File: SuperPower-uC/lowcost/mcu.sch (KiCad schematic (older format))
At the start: 5 parts, among them J5 main pin header right, J6 main pin header left, U13 ESP32-WROOM32

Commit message: moved connector over to mcu sheet, made some vias smaller ...
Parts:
- removed J5: main pin header right, Connector_PinHeader_2.54mm:PinHeader_1x17_P2.54mm_Vertical, symbol Connector:Conn_01x17_Female
- removed J6: main pin header left, Connector_PinHeader_2.54mm:PinHeader_1x17_P2.54mm_Vertical, symbol Connector:Conn_01x17_Female
- added J5: main pin header fight, Connector_PinSocket_2.54mm:PinSocket_1x21_P2.54mm_Vertical, symbol Connector:Conn_01x21_Female
- added J6: main pin header left, Connector_PinSocket_2.54mm:PinSocket_1x21_P2.54mm_Vertical, symbol Connector:Conn_01x21_Female
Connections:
- net labels added: 3v3_EN, 5V_EN, CH_DIS, INT_IO, exp4, exp5, exp6, exp7
- wire segments 83 -> 91
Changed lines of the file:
@@
 IO23
 Wire Wire Line
-	9800 3250 9600 3250
-Wire Wire Line
-	9800 3350 9600 3350
-Wire Wire Line
-	9800 3450 9600 3450
-Wire Wire Line
-	9800 3550 9600 3550
-Wire Wire Line
-	9800 3650 9600 3650
-Wire Wire Line
-	9800 3750 9600 3750
-Wire Wire Line
-	9800 3950 9600 3950
-Wire Wire Line
-	9600 3850 9800 3850
-Wire Wire Line
-	9800 4050 9600 4050
-Wire Wire Line
-	9600 4150 9800 4150
-Wire Wire Line
-	9600 4250 9800 4250
-Text Label 9600 3250 0    50   ~ 0
+	9900 3550 9700 3550
+Wire Wire Line
+	9900 3650 9700 3650
+Wire Wire Line
+	9900 3750 9700 3750
+Wire Wire Line
+	9900 3850 9700 3850
+Wire Wire Line
+	9900 3950 9700 3950
+Wire Wire Line
+	9900 4050 9700 4050
+Wire Wire Line
+	9900 4250 9700 4250
+Wire Wire Line
+	9700 4150 9900 4150
+Wire Wire Line
+	9900 4350 9700 4350
+Wire Wire Line
+	9700 4450 9900 4450
+Wire Wire Line
+	9700 4550 9900 4550
+Text Label 9700 3550 0    50   ~ 0
 IO36
-Text Label 9600 3350 0    50   ~ 0
+Text Label 9700 3650 0    50   ~ 0
 IO39
-Text Label 9600 3450 0    50   ~ 0
+Text Label 9700 3750 0    50   ~ 0
 IO34
-Text Label 9600 3550 0    50   ~ 0
+Text Label 9700 3850 0    50   ~ 0
 IO35
-Text Label 9600 3650 0    50   ~ 0
+Text Label 9700 3950 0    50   ~ 0
 IO32
-Text Label 9600 3750 0    50   ~ 0
+Text Label 9700 4050 0    50   ~ 0
 IO33
-Text Label 9600 3850 0    50   ~ 0
+Text Label 9700 4150 0    50   ~ 0
 IO25
-Text Label 9600 3950 0    50   ~ 0
+Text Label 9700 4250 0    50   ~ 0
 IO26
-Text Label 9600 4050 0    50   ~ 0
+Text Label 9700 4350 0    50   ~ 0
 IO27
-Text Label 9600 4150 0    50   ~ 0
+Text Label 9700 4450 0    50   ~ 0
 IO14
-Text Label 9600 4250 0    50   ~ 0
+Text Label 9700 4550 0    50   ~ 0
 IO12
 Wire Wire Line
-	9800 4350 9600 4350
-Text Label 9600 4350 0    50   ~ 0
+	9900 4650 9700 4650
+Text Label 9700 4650 0    50   ~ 0
 IO13
 Wire Wire Line
-	9800 4450 9250 4450
+	9900 4750 9350 4750
 $Comp
 L power:GND #PWR0120
 U 1 1 5F8C9F4B
-P 9250 4450
-F 0 "#PWR0120" H 9250 4200 50  0001 C CNN
-F 1 "GND" H 9255 4277 50  0000 C CNN
-F 2 "" H 9250 4450 50  0001 C CNN
-F 3 "" H 9250 4450 50  0001 C CNN
-	1    9250 4450
-	1    0    0    -1
-$EndComp
-Wire Wire Line
-	9600 1250 9800 1250
-Wire Wire Line
-	9600 1350 9800 1350
-Wire Wire Line
-	9600 1450 9800 1450
-Wire Wire Line
-	9600 1550 9800 1550
-Wire Wire Line
-	9600 1650 9800 1650
-Wire Wire Line
-	9600 1750 9800 1750
-Wire Wire Line
-	9600 1850 9800 1850
-Wire Wire Line
-	9600 1950 9800 1950
-Wire Wire Line
-	9600 2050 9800 2050
-Wire Wire Line
-	9600 2150 9800 2150
-Wire Wire Line
-	9600 2250 9800 2250
-Wire Wire Line
-	9600 1150 9800 1150
-Text Label 9600 1150 0    50   ~ 0
+P 9350 4750
+F 0 "#PWR0120" H 9350 4500 50  0001 C CNN
+F 1 "GND" H 9355 4577 50  0000 C CNN
+F 2 "" H 9350 4750 50  0001 C CNN
+F 3 "" H 9350 4750 50  0001 C CNN
+	1    9350 4750
+	1    0    0    -1
+$EndComp
+Wire Wire Line
+	9700 1150 9900 1150
+Wire Wire Line
+	9700 1250 9900 1250
+Wire Wire Line
+	9700 1350 9900 1350
+Wire Wire Line
+	9700 1450 9900 1450
+Wire Wire Line
+	9700 1550 9900 1550
+Wire Wire Line
+	9700 1650 9900 1650
+Wire Wire Line
+	9700 1750 9900 1750
+Wire Wire Line
+	9700 1850 9900 1850
+Wire Wire Line
+	9700 1950 9900 1950
+Wire Wire Line
+	9700 2050 9900 2050
+Wire Wire Line
+	9700 2150 9900 2150
+Wire Wire Line
+	9700 1050 9900 1050
+Text Label 9700 1050 0    50   ~ 0
 IO0
-Text Label 9600 2250 0    50   ~ 0
+Text Label 9700 2150 0    50   ~ 0
 IO4
-Text Label 9600 2150 0    50   ~ 0
+Text Label 9700 2050 0    50   ~ 0
 IO16
-Text Label 9600 2050 0    50   ~ 0
+Text Label 9700 1950 0    50   ~ 0
 IO17
-Text Label 9600 1950 0    50   ~ 0
+Text Label 9700 1850 0    50   ~ 0
 IO5
-Text Label 9600 1850 0    50   ~ 0
+Text Label 9700 1750 0    50   ~ 0
 IO18
-Text Label 9600 1750 0    50   ~ 0
+Text Label 9700 1650 0    50   ~ 0
 IO19
-Text Label 9600 1650 0    50   ~ 0
+Text Label 9700 1550 0    50   ~ 0
 IO21
-Text Label 9600 1550 0    50   ~ 0
+Text Label 9700 1450 0    50   ~ 0
 RX
-Text Label 9600 1450 0    50   ~ 0
+Text Label 9700 1350 0    50   ~ 0
 TX
-Text Label 9600 1350 0    50   ~ 0
+Text Label 9700 1250 0    50   ~ 0
 IO22
-Text Label 9600 1250 0    50   ~ 0
+Text Label 9700 1150 0    50   ~ 0
 IO23
 Wire Wire Line
-	9800 2350 9600 2350
-Text Label 9600 2350 0    50   ~ 0
+	9900 2250 9700 2250
+Text Label 9700 2250 0    50   ~ 0
 IO2
 Text Label 1250 1150 0    50   ~ 0
@@
 	1150 1750 1250 1750
 Wire Wire Line
-	9800 2450 9600 2450
-Text Label 9600 2450 0    50   ~ 0
+	9900 2350 9700 2350
+Text Label 9700 2350 0    50   ~ 0
 IO15
 Text HLabel 1100 2200 0    50   Input ~ 0
@@
 	11000 700  9000 700
 Wire Notes Line
-	9000 700  9000 5000
-Wire Notes Line
-	9000 5000 11000 5000
-Wire Notes Line
-	11000 700  11000 5000
+	9000 5450 11000 5450
 Wire Notes Line
 	3400 2300 8000 2300
@@
 Text Notes 3500 2450 0    50   ~ 0
 MCU
-Text Label 9400 4650 0    50   ~ 0
+Text Label 9500 4950 0    50   ~ 0
 5V
 Wire Wire Line
-	9800 2650 9400 2650
-Text Label 9400 2650 0    50   ~ 0
+	9900 2550 9500 2550
+Text Label 9500 2550 0    50   ~ 0
 3v3_MCU
 Text Label 3950 3250 0    50   ~ 0
@@
 5V
 Wire Wire Line
-	9400 4650 9800 4650
+	9500 4950 9900 4950
 Wire Notes Line
 	600  650  1850 650
@@
 Text Notes 9100 850  0    50   ~ 0
 Main pin Headers\n
-Text Label 9600 3150 0    50   ~ 0
+Text Label 9700 3450 0    50   ~ 0
 RST
 Wire Wire Line
-	9600 3150 9800 3150
-Wire Wire Line
-	9800 2550 9250 2550
+	9700 3450 9900 3450
+Wire Wire Line
+	9900 2450 9350 2450
 $Comp
 L power:GND #PWR0119
 U 1 1 5F8D40E5
-P 9250 2550
-F 0 "#PWR0119" H 9250 2300 50  0001 C CNN
-F 1 "GND" H 9255 2377 50  0000 C CNN
-F 2 "" H 9250 2550 50  0001 C CNN
-F 3 "" H 9250 2550 50  0001 C CNN
-	1    9250 2550
-	1    0    0    -1
-$EndComp
-$Comp
-L Connector:Conn_01x17_Female J5
-U 1 1 5F904645
-P 10000 1950
-F 0 "J5" H 10028 1976 50  0000 L CNN
-F 1 "main pin header right" H 10028 1885 50  0000 L CNN
-F 2 "Connector_PinHeader_2.54mm:PinHeader_1x17_P2.54mm_Vertical" H 10000 1950 50  0001 C CNN
-F 3 "~" H 10000 1950 50  0001 C CNN
-	1    10000 1950
-	1    0    0    -1
-$EndComp
-$Comp
-L Connector:Conn_01x17_Female J6
-U 1 1 5F90988E
-P 10000 3850
-F 0 "J6" H 10028 3876 50  0000 L CNN
-F 1 "main pin header left" H 10028 3785 50  0000 L CNN
-F 2 "Connector_PinHeader_2.54mm:PinHeader_1x17_P2.54mm_Vertical" H 10000 3850 50  0001 C CNN
-F 3 "~" H 10000 3850 50  0001 C CNN
-	1    10000 3850
-	1    0    0    -1
-$EndComp
-Text Label 9400 4550 0    50   ~ 0
+P 9350 2450
+F 0 "#PWR0119" H 9350 2200 50  0001 C CNN
+F 1 "GND" H 9355 2277 50  0000 C CNN
+F 2 "" H 9350 2450 50  0001 C CNN
+F 3 "" H 9350 2450 50  0001 C CNN
+	1    9350 2450
+	1    0    0    -1
+$EndComp
+Text Label 9500 4850 0    50   ~ 0
 Vin
 Wire Wire Line
-	9400 4550 9800 4550
+	9500 4850 9900 4850
 Text HLabel 1100 2400 0    50   Output ~ 0
 Vin
@@
 Vin
 Wire Wire Line
-	9400 2750 9800 2750
-Text Label 9400 2750 0    50   ~ 0
+	9500 2650 9900 2650
+Text Label 9500 2650 0    50   ~ 0
 3v3
 Wire Wire Line
-	9800 3050 9250 3050
+	9900 3350 9350 3350
 $Comp
 L power:GND #PWR0128
 U 1 1 5F982B4C
-P 9250 3050
-F 0 "#PWR0128" H 9250 2800 50  0001 C CNN
-F 1 "GND" H 9255 2877 50  0000 C CNN
-F 2 "" H 9250 3050 50  0001 C CNN
-F 3 "" H 9250 3050 50  0001 C CNN
-	1    9250 3050
-	1    0    0    -1
-$EndComp
+P 9350 3350
+F 0 "#PWR0128" H 9350 3100 50  0001 C CNN
+F 1 "GND" H 9355 3177 50  0000 C CNN
+F 2 "" H 9350 3350 50  0001 C CNN
+F 3 "" H 9350 3350 50  0001 C CNN
+	1    9350 3350
+	1    0    0    -1
+$EndComp
+Wire Notes Line
+	9000 700  9000 5450
+Wire Notes Line
+	11000 700  11000 5450
+$Comp
+L Connector:Conn_01x21_Female J5
+U 1 1 5FA06BF5
+P 10100 2050
+F 0 "J5" H 10128 2076 50  0000 L CNN
+F 1 "main pin header fight" H 10128 1985 50  0000 L CNN
+F 2 "Connector_PinSocket_2.54mm:PinSocket_1x21_P2.54mm_Vertical" H 10100 2050 50  0001 C CNN
+F 3 "~" H 10100 2050 50  0001 C CNN
+	1    10100 2050
+	1    0    0    -1
+$EndComp
+Wire Wire Line
+	9850 2750 9900 2750
+Wire Wire Line
+	9900 2850 9850 2850
+Wire Wire Line
+	9850 2950 9900 2950
+Wire Wire Line
+	9900 3050 9850 3050
+Wire Wire Line
+	9850 5050 9900 5050
+Wire Wire Line
+	9850 5350 9900 5350
+Wire Wire Line
+	9850 5150 9900 5150
+$Comp
+L Connector:Conn_01x21_Female J6
+U 1 1 5FA047AE
+P 10100 4350
+F 0 "J6" H 10128 4376 50  0000 L CNN
+F 1 "main pin header left" H 10128 4285 50  0000 L CNN
+F 2 "Connector_PinSocket_2.54mm:PinSocket_1x21_P2.54mm_Vertical" H 10100 4350 50  0001 C CNN
+F 3 "~" H 10100 4350 50  0001 C CNN
+	1    10100 4350
+	1    0    0    -1
+$EndComp
+Text GLabel 9850 5050 0    50   Input ~ 0
+INT_IO
+Text GLabel 9850 5150 0    50   Input ~ 0
+3v3_EN
+Text GLabel 9850 5250 0    50   Input ~ 0
+5V_EN
+Text GLabel 9850 5350 0    50   Input ~ 0
+CH_DIS
+Wire Wire Line
+	9850 5250 9900 5250
+Text GLabel 9850 2750 0    50   Input ~ 0
+exp7
+Text GLabel 9850 2850 0    50   Input ~ 0
+exp6
+Text GLabel 9850 2950 0    50   Input ~ 0
+exp5
+Text GLabel 9850 3050 0    50   Input ~ 0
+exp4
 $EndSCHEMATC

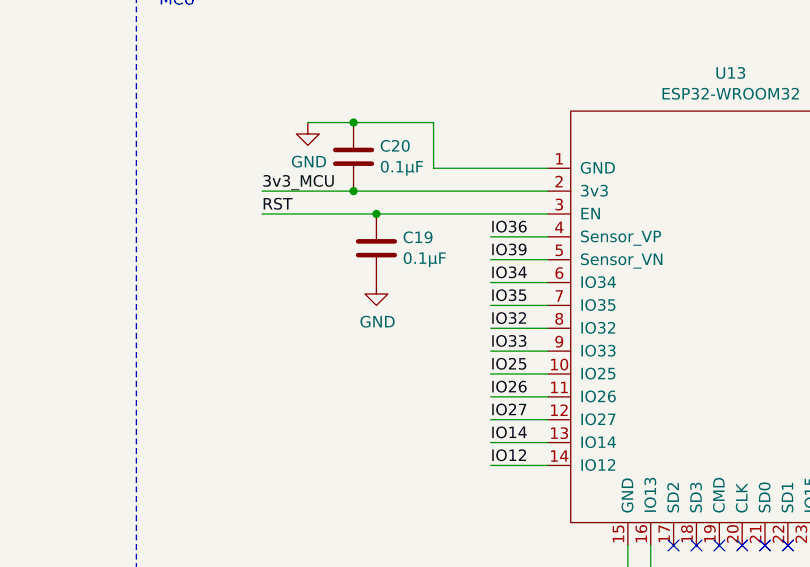
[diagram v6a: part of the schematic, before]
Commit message: added rst pullup
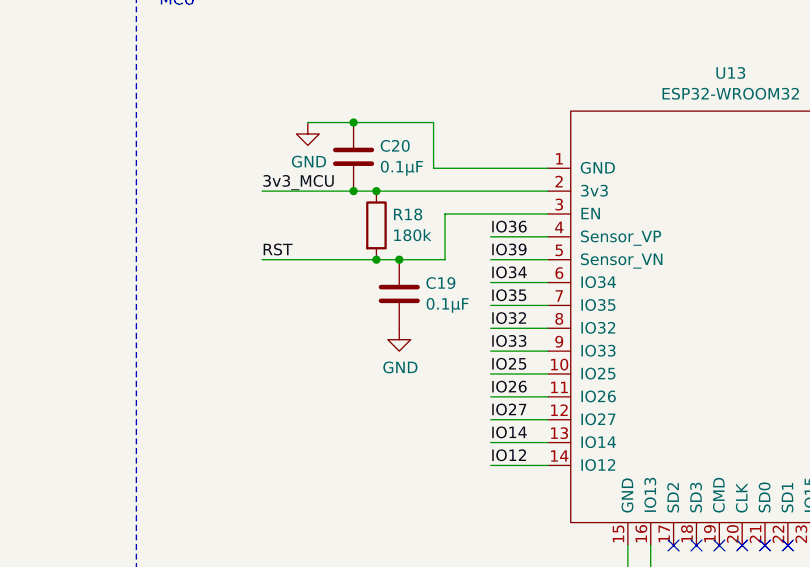
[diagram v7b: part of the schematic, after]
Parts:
- added R18: 180k, Resistor_SMD:R_0603_1608Metric_Pad1.05x0.95mm_HandSolder, symbol Device:R
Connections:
- wire segments 91 -> 95
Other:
- moved on the sheet: C19
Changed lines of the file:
@@
 GPIO0
 Wire Wire Line
-	5200 3250 4350 3250
+	5200 3250 4450 3250
 Wire Wire Line
 	5200 3450 4950 3450
@@
 L Device:C C19
 U 1 1 5F8B82D1
-P 4450 3500
-F 0 "C19" H 4565 3546 50  0000 L CNN
-F 1 "0.1µF" H 4565 3455 50  0000 L CNN
-F 2 "Capacitor_SMD:C_0603_1608Metric_Pad1.05x0.95mm_HandSolder" H 4488 3350 50  0001 C CNN
-F 3 "~" H 4450 3500 50  0001 C CNN
-F 4 "C14858" H 4450 3500 50  0001 C CNN "LCSC"
-	1    4450 3500
-	1    0    0    -1
-$EndComp
-Connection ~ 4450 3350
-Wire Wire Line
-	4450 3350 5200 3350
+P 4550 3700
+F 0 "C19" H 4665 3746 50  0000 L CNN
+F 1 "0.1µF" H 4665 3655 50  0000 L CNN
+F 2 "Capacitor_SMD:C_0603_1608Metric_Pad1.05x0.95mm_HandSolder" H 4588 3550 50  0001 C CNN
+F 3 "~" H 4550 3700 50  0001 C CNN
+F 4 "C14858" H 4550 3700 50  0001 C CNN "LCSC"
+	1    4550 3700
+	1    0    0    -1
+$EndComp
 $Comp
 L power:GND #PWR0117
 U 1 1 5F8BCADF
-P 4450 3650
-F 0 "#PWR0117" H 4450 3400 50  0001 C CNN
-F 1 "GND" H 4455 3477 50  0000 C CNN
-F 2 "" H 4450 3650 50  0001 C CNN
-F 3 "" H 4450 3650 50  0001 C CNN
-	1    4450 3650
+P 4550 3850
+F 0 "#PWR0117" H 4550 3600 50  0001 C CNN
+F 1 "GND" H 4555 3677 50  0000 C CNN
+F 2 "" H 4550 3850 50  0001 C CNN
+F 3 "" H 4550 3850 50  0001 C CNN
+	1    4550 3850
 	1    0    0    -1
 $EndComp
@@
 Text Label 1250 1850 0    50   ~ 0
 RST
-Text Label 3950 3350 0    50   ~ 0
+Text Label 3950 3550 0    50   ~ 0
 RST
-Wire Wire Line
-	3950 3350 4450 3350
 Text Label 1250 2300 0    50   ~ 0
 3v3
@@
 Text GLabel 9850 3050 0    50   Input ~ 0
 exp4
+$Comp
+L Device:R R18
+U 1 1 5FC9B88E
+P 4450 3400
+F 0 "R18" H 4520 3446 50  0000 L CNN
+F 1 "180k" H 4520 3355 50  0000 L CNN
+F 2 "Resistor_SMD:R_0603_1608Metric_Pad1.05x0.95mm_HandSolder" V 4380 3400 50  0001 C CNN
+F 3 "~" H 4450 3400 50  0001 C CNN
+F 4 "C22827" H 4450 3400 50  0001 C CNN "LCSC"
+	1    4450 3400
+	1    0    0    -1
+$EndComp
+Connection ~ 4450 3250
+Wire Wire Line
+	4450 3250 4350 3250
+Wire Wire Line
+	5200 3350 4750 3350
+Wire Wire Line
+	4750 3350 4750 3550
+Wire Wire Line
+	4750 3550 4550 3550
+Connection ~ 4450 3550
+Wire Wire Line
+	4450 3550 3950 3550
+Connection ~ 4550 3550
+Wire Wire Line
+	4550 3550 4450 3550
 $EndSCHEMATC

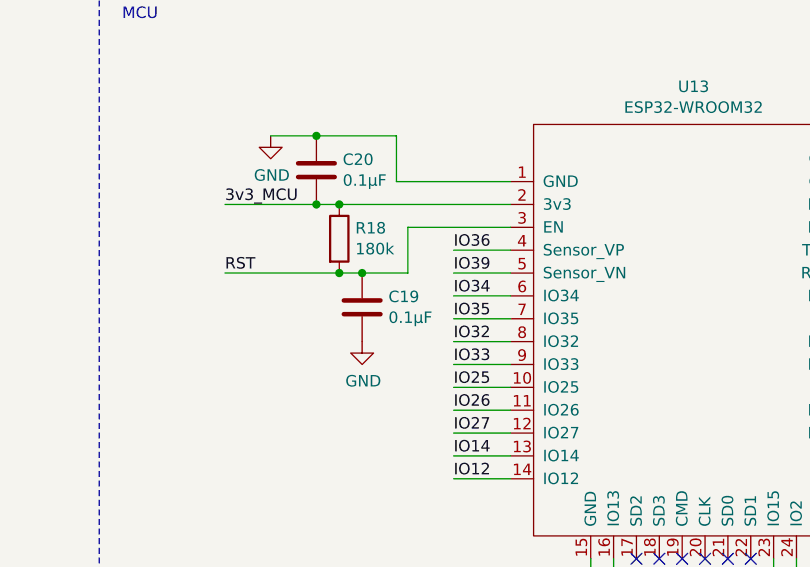
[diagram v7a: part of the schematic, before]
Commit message: added proper high side cutoff for 5v regulator
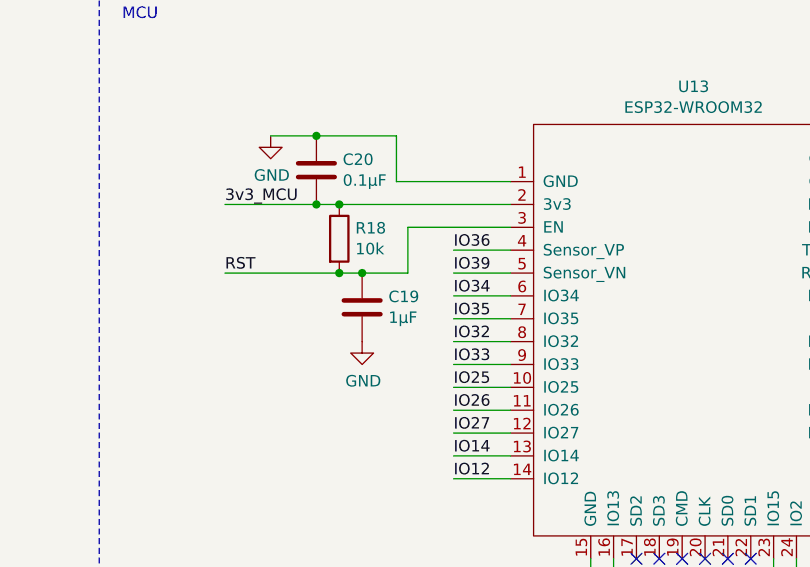
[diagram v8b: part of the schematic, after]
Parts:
- C19: value 0.1µF -> 1µF; LCSC C14858 -> C15849
- R18: value 180k -> 10k; LCSC C22827 -> C25804
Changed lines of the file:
@@
 P 4550 3700
 F 0 "C19" H 4665 3746 50  0000 L CNN
-F 1 "0.1µF" H 4665 3655 50  0000 L CNN
+F 1 "1µF" H 4665 3655 50  0000 L CNN
 F 2 "Capacitor_SMD:C_0603_1608Metric_Pad1.05x0.95mm_HandSolder" H 4588 3550 50  0001 C CNN
 F 3 "~" H 4550 3700 50  0001 C CNN
-F 4 "C14858" H 4550 3700 50  0001 C CNN "LCSC"
+F 4 "C15849" H 4550 3700 50  0001 C CNN "LCSC"
 	1    4550 3700
 	1    0    0    -1
@@
 P 4450 3400
 F 0 "R18" H 4520 3446 50  0000 L CNN
-F 1 "180k" H 4520 3355 50  0000 L CNN
+F 1 "10k" H 4520 3355 50  0000 L CNN
 F 2 "Resistor_SMD:R_0603_1608Metric_Pad1.05x0.95mm_HandSolder" V 4380 3400 50  0001 C CNN
 F 3 "~" H 4450 3400 50  0001 C CNN
-F 4 "C22827" H 4450 3400 50  0001 C CNN "LCSC"
+F 4 "C25804" H 4450 3400 50  0001 C CNN "LCSC"
 	1    4450 3400
 	1    0    0    -1
